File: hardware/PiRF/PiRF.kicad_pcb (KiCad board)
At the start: 2 copper layers, 65 x 56 mm, 54 parts, among them J1 CONN_01X02, J2 40HAT, J3 Conn_02x20_Odd_Even, J4 CONN_01X02, J5 Conn_Coaxial, J6 CONN_01X02, Q1 MMBT3904, U1 CAT24C32, U2 TPS7A19, U3 TS5A23159, U4 TPS2294x, U5 ST_Teseo

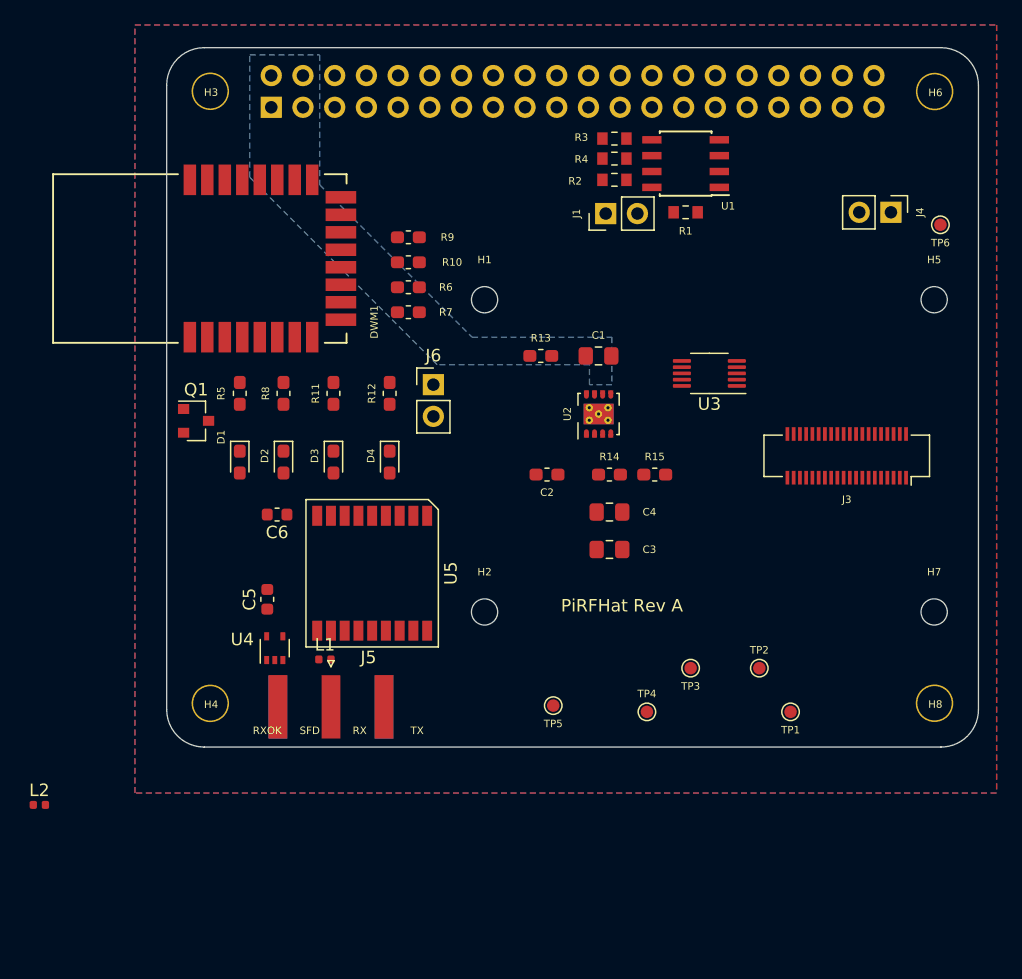
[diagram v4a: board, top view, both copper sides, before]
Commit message: Removed the DWM1000 and replaced it with GPS.
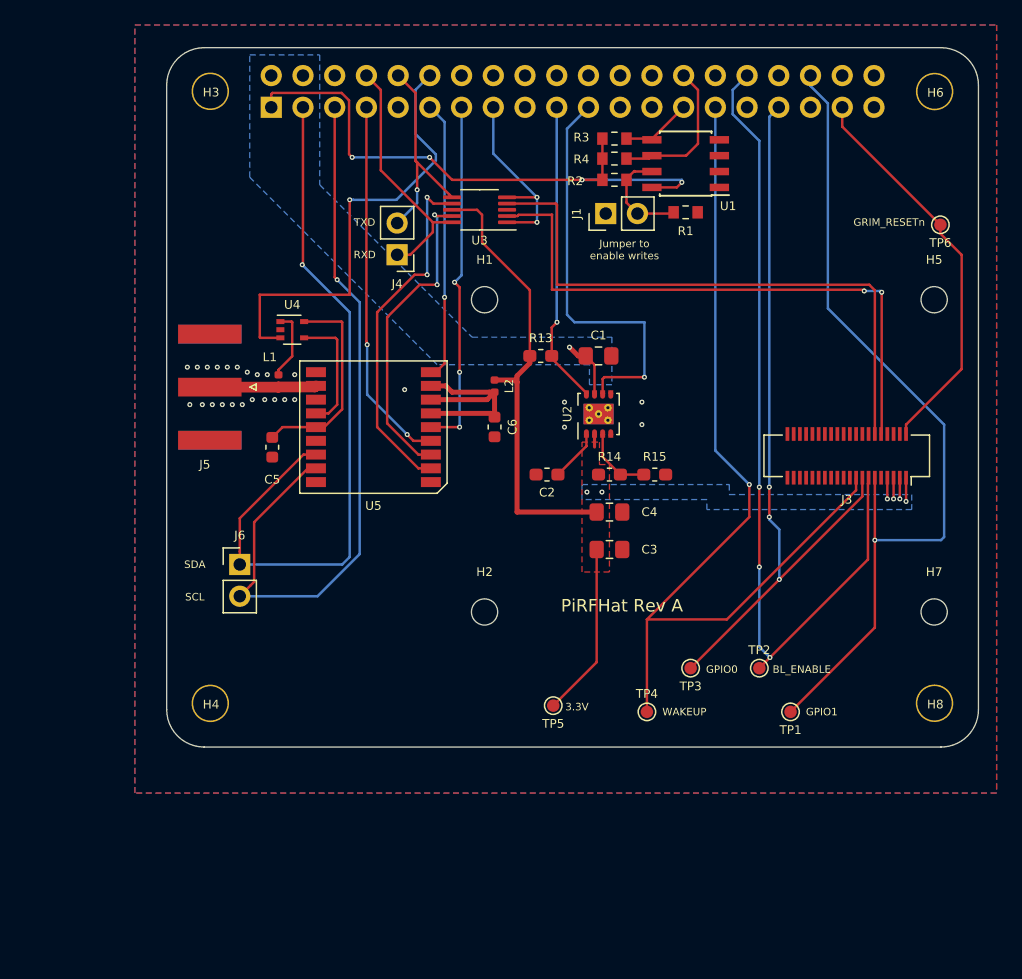
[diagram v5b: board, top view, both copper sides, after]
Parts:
- removed D1, D2, D3, D4: LED, LED_SMD:LED_0603_1608Metric_Pad1.05x0.95mm_HandSolder
- removed DWM1: DWM1000, RF_Module:DWM1000
- removed Q1: MMBT3904, Package_TO_SOT_SMD:SOT-23
- removed R10, R7: 0, Resistor_SMD:R_0603_1608Metric_Pad1.05x0.95mm_HandSolder
- removed R11, R12, R5, R8: 1.5k, Resistor_SMD:R_0603_1608Metric_Pad1.05x0.95mm_HandSolder
- removed R6, R9: DNP, Resistor_SMD:R_0603_1608Metric_Pad1.05x0.95mm_HandSolder
- moved L2 49.5 mm to (104.8, 87.9), turned to 270 degrees
- moved J4 39.7 mm to (97.0, 77.4), turned to 180 degrees
- moved J5 27.4 mm to (82.0, 88.0), turned to 180 degrees
- moved U4 25.5 mm to (88.6, 83.4), turned to 0 degrees
- moved L1 22.6 mm to (87.5, 87.5), turned to 270 degrees
- moved U3 22.6 mm to (103.6, 73.8)
- moved J6 21.2 mm to (84.4, 102.2)
- moved C6 18.8 mm to (104.8, 91.2), turned to 270 degrees
- moved C5 12.2 mm to (87.0, 92.8), turned to 270 degrees
- moved U5 11.7 mm to (95.1, 91.2), turned to 90 degrees
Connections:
- J2 pad 11: /HAT_PG -> /GPS_RESETn
- J2 pad 12: (no net) -> /GPS_ANT_OC
- J2 pad 13: /HAT_PWR_EN -> /GPS_WAKE
- J2 pad 15: /GPS_PPS -> /UART_MUX
- J2 pad 17: /GPS_RESETn -> (no net)
- J2 pad 19: /GPS_WAKE -> /HAT_PG
- J2 pad 21: /UART_MUX -> /HAT_PWR_EN
- J2 pad 23: /GPS_ANT_OC -> (no net)
- J2 pad 24: /SS -> (no net)
- J2 pad 35: /MISO -> (no net)
- J2 pad 38: /MOSI -> (no net)
- J2 pad 40: /SCLK -> (no net)
- J2 pad 7: /UWB_RSTn -> /GPS_PPS
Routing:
- net /WAKEUP: track 0.00 -> 75.0 mm, vias 0 -> 1
- net /GPIO1: track 0.00 -> 68.6 mm, vias 0 -> 1
- net /BL_ENABLE: track 0.00 -> 67.2 mm, vias 0 -> 3
- net /GPS_SCL: track 0.00 -> 60.7 mm, vias 0 -> 1
- net /GPIO0: track 0.00 -> 59.5 mm, vias 0 -> 3
- net +3V3: track 0.00 -> 58.7 mm, vias 0 -> 6
- net /GPS_SDA: track 0.00 -> 58.6 mm, vias 0 -> 1
- net /GRIM_TXD: track 0.00 -> 47.6 mm
- net /GRIM_RXD: track 0.00 -> 47.6 mm, vias 0 -> 2
- net /HAT_3V3: track 0.00 -> 47.1 mm, vias 0 -> 4
- net /GPS_ANT_OC: track 0.00 -> 36.0 mm, vias 0 -> 1
- net /HAT_PWR_EN: track 0.00 -> 32.8 mm, vias 0 -> 1
- net /RESET_N: track 0.00 -> 32.0 mm
- net /GPS_PPS: track 0.00 -> 29.6 mm, vias 0 -> 2
- net /GPS_TXD: track 0.00 -> 28.5 mm, vias 0 -> 2
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- added copper zone on B.Cu, net +3V3
- added copper zone on F.Cu, net +3V3
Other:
- board text added: "3.3V"
- board text added: "BL_ENABLE"
- board text added: "GPIO0"
- board text added: "GPIO1"
- board text added: "GRIM_RESETn"
- board text added: "Jumper to enable writes"
- board text added: "RXD"
- board text added: "SCL"
- board text added: "SDA"
- board text added: "TXD"
- board text added: "WAKEUP"
- board text removed: "RX"
- board text removed: "RXOK"
- board text removed: "SFD"
- board text removed: "TX"

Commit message: Added an info section to the silkscreen.
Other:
- board text added: "PiRFHat-GPS Rev A Nick Butts Copyright 2019"
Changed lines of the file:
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@@
   (general
     (thickness 1.6)
-    (drawings 66)
+    (drawings 67)
     (tracks 331)
     (zones 0)
@@
   )
   (setup
-    (last_trace_width 0.153)
+    (last_trace_width 0.15)
     (user_trace_width 0.153)
     (user_trace_width 0.2)
@@
       (clearance 1.6))
   )
+  (gr_text "PiRFHat-GPS\nRev A\nNick Butts\nCopyright 2019 " (at 95.2 111.2) (layer B.SilkS)
+    (effects (font (size 1 1) (thickness 0.25)) (justify mirror))
+  )
   (gr_text 3.3V (at 111.4 113.6) (layer F.SilkS)

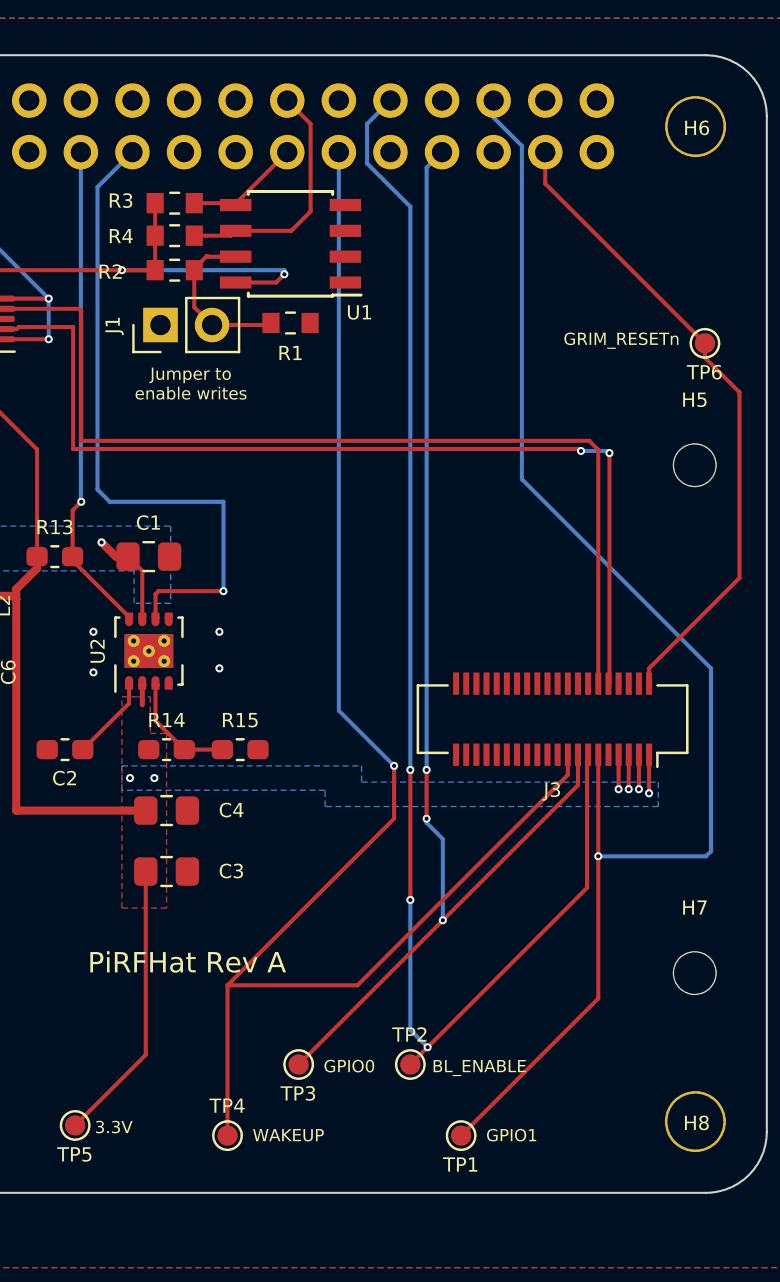
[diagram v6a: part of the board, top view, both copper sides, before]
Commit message: Added a cutout for the camera.
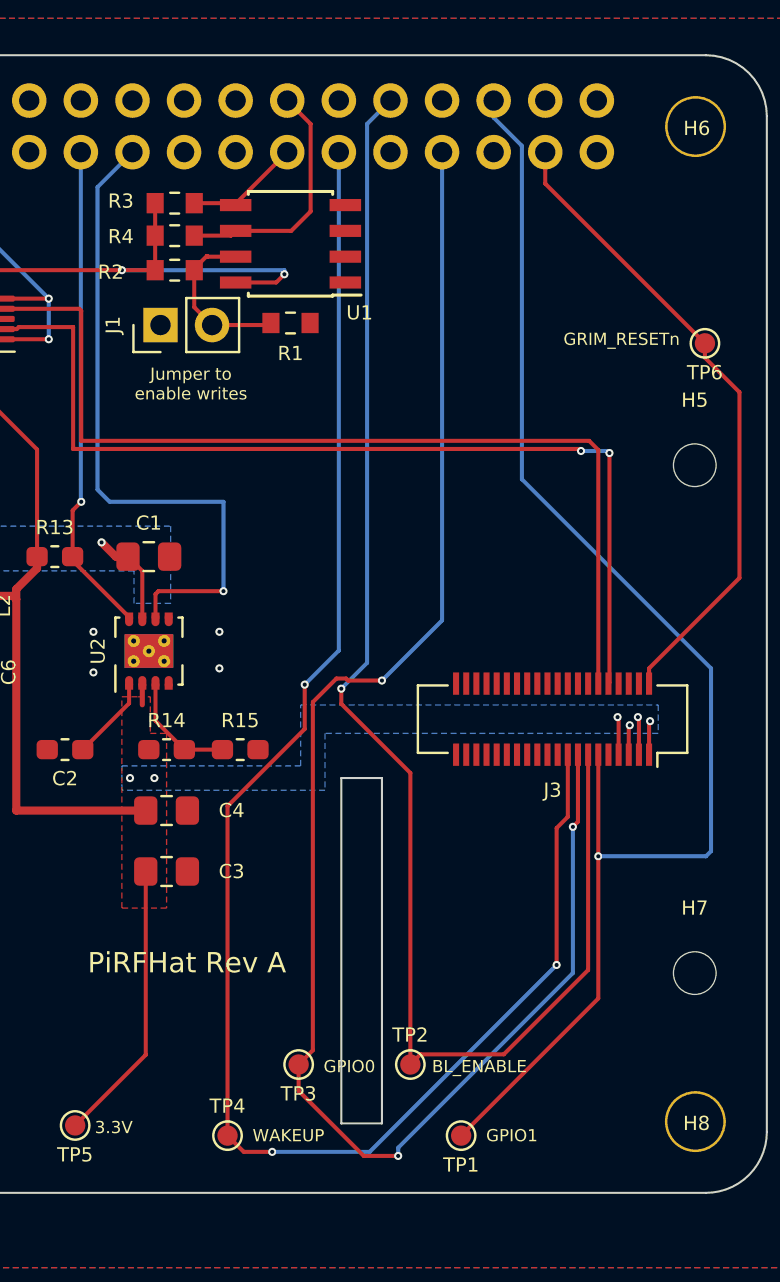
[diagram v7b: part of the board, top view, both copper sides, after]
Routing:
- net /GPIO0: track 59.5 -> 80.2 mm
- net /WAKEUP: track 75.0 -> 81.6 mm, vias 1 -> 3
- net /BL_ENABLE: track 67.2 -> 71.1 mm, vias 3 -> 1
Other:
- outline, holes or cut-outs redrawn

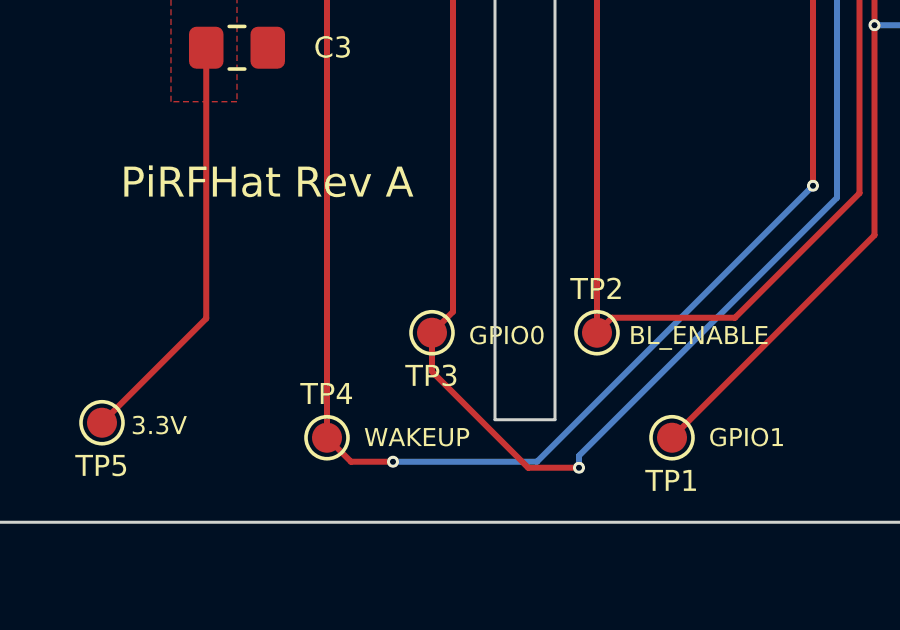
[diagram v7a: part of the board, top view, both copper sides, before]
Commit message: Update part numbers.
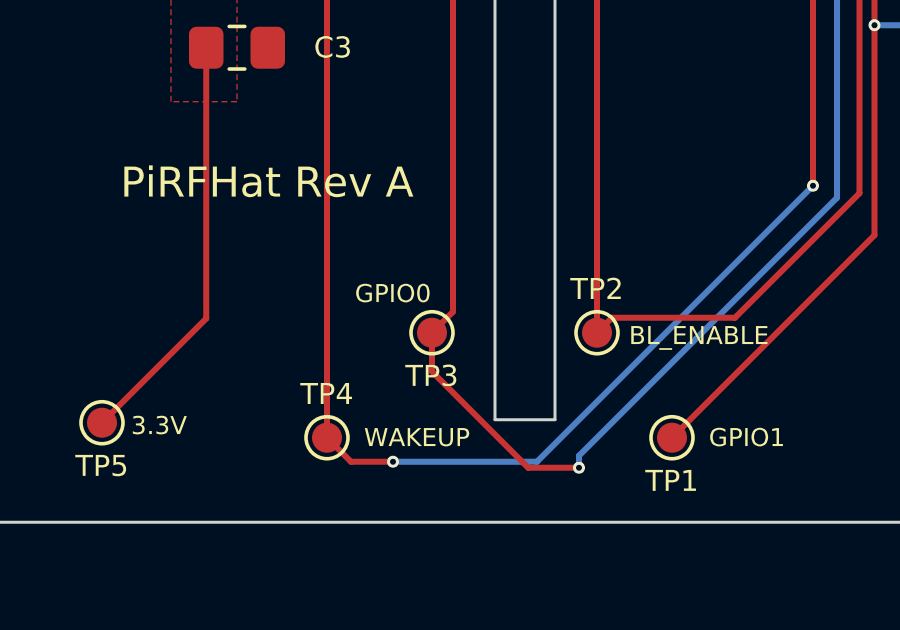
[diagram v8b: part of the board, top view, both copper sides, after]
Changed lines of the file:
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@@
     (effects (font (size 0.6 0.6) (thickness 0.09)))
   )
-  (gr_text GPIO0 (at 123 110.6) (layer F.SilkS)
+  (gr_text GPIO0 (at 119.2 109.2) (layer F.SilkS)
     (effects (font (size 0.6 0.6) (thickness 0.09)))
   )
